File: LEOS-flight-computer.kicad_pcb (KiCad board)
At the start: 2 copper layers, 100 x 100 mm, 24 parts, among them J1 MicroFit_1x4, J2 MicroFit_1x4, J3 GPIO, J4 I2C Breakout, J5 SPI Breakout, U1 MCP2562FD, U2 MCP2518FD, Y1 40 MHz

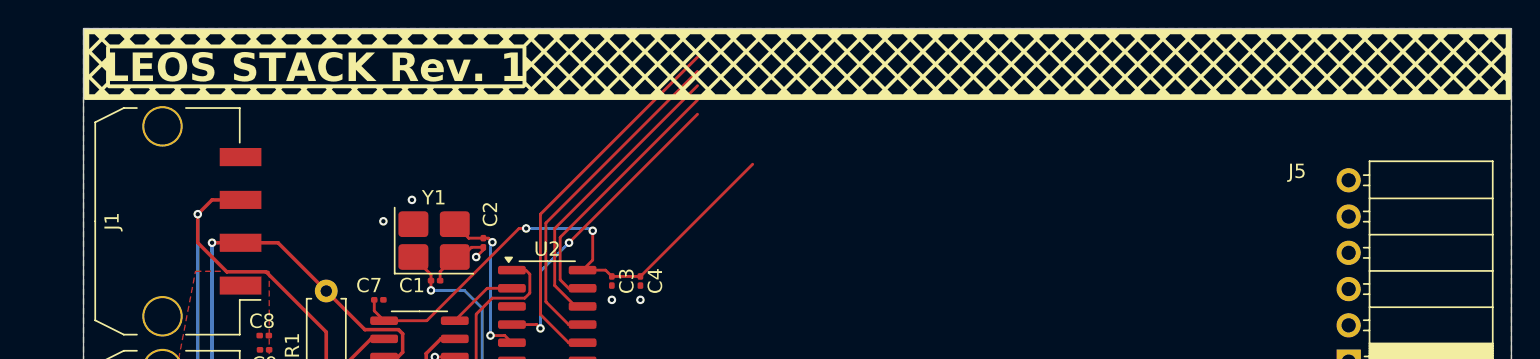
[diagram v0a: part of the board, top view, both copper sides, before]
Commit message: Change Silkscreen name to flight computer
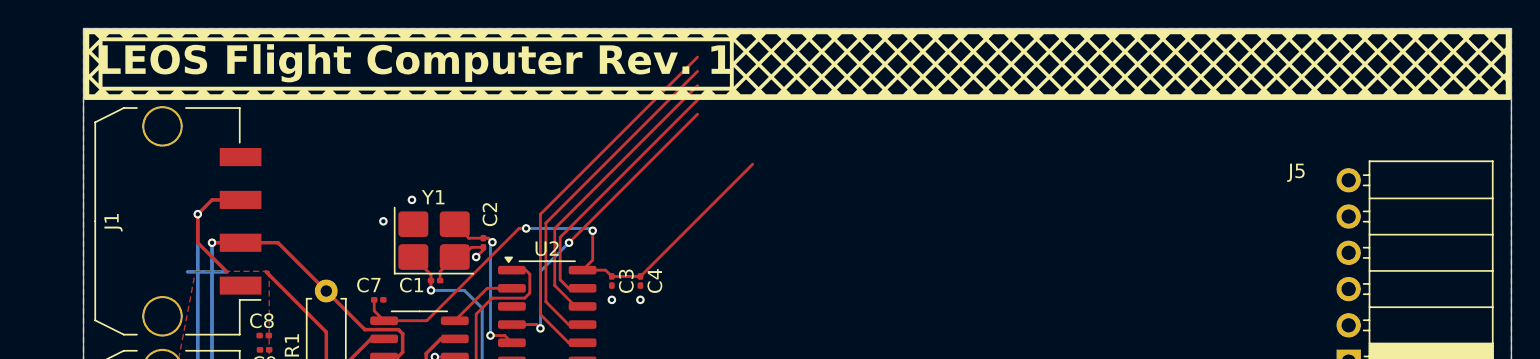
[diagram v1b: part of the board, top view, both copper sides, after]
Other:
- board text added: "LEOS Flight Computer Rev. 1"
- board text removed: "LEOS STACK Rev. 1"
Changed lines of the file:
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@@
 		(layer "Edge.Cuts")
 	)
-	(gr_text "LEOS STACK Rev. 1"
-		(at 116.25 52.75 0)
+	(gr_text "LEOS Flight Computer Rev. 1"
+		(at 123.25 52.25 0)
 		(layer "F.SilkS" knockout)
 		(effects
@@
 	)
 	(segment
-		(start 110.039 67.039)
-		(end 112.786 67.039)
-		(width 0.25)
-		(layer "F.Cu")
-		(net 12)
-	)
-	(segment
 		(start 108 65)
 		(end 110.039 67.039)
@@
 		(net 12)
 	)
+	(segment
+		(start 110.039 67.039)
+		(end 107.292 67.039)
+		(width 0.25)
+		(layer "B.Cu")
+		(net 12)
+	)

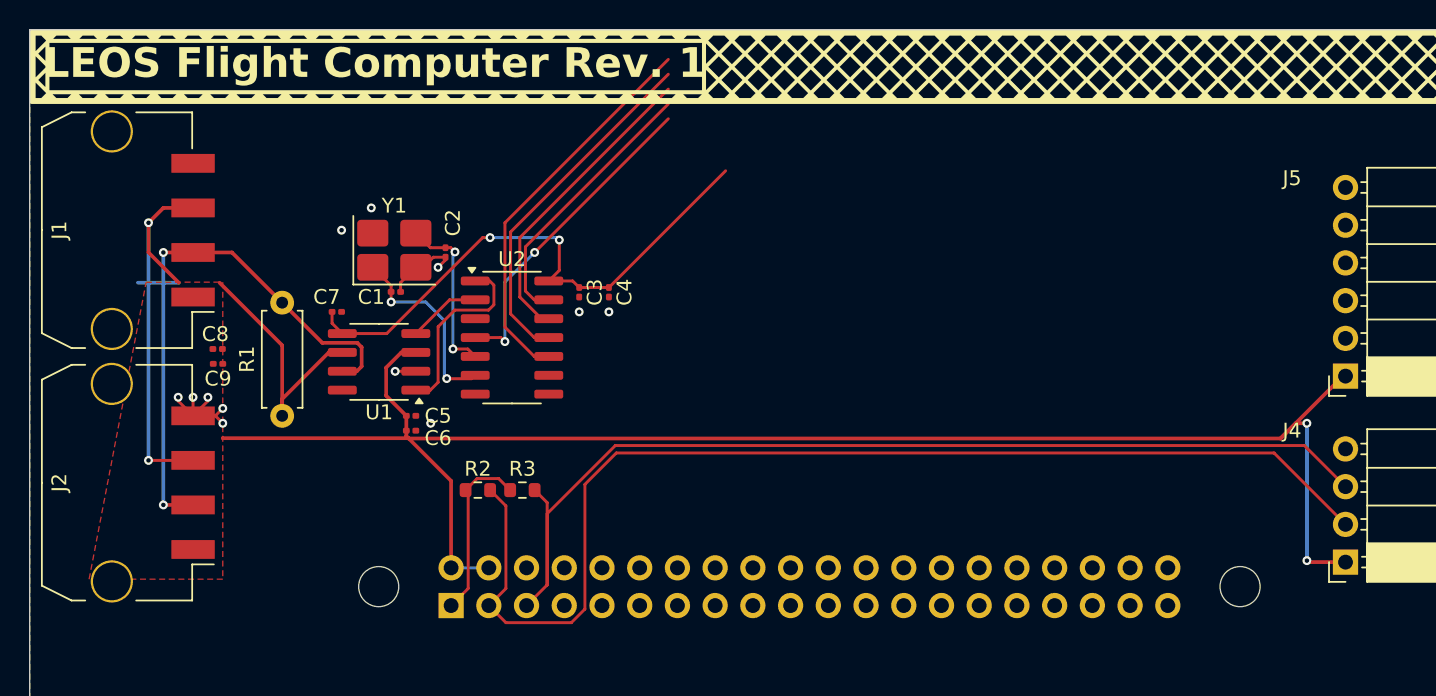
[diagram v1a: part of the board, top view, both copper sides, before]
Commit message: Corrected layout for flight computer with breakout headers routed
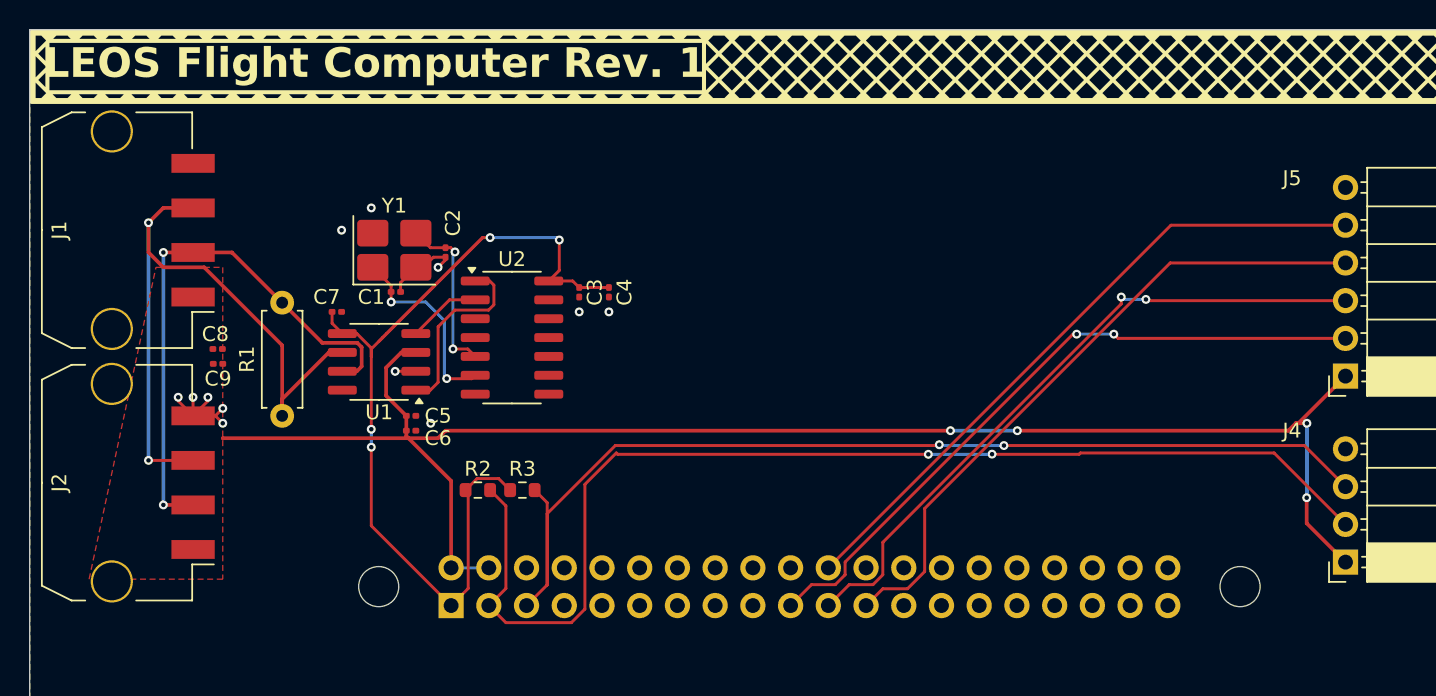
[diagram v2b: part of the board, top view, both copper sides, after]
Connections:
- J5 pad 3: GPIO09.SPI0/MISO -> GPIO9/SPI0.MISO
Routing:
- net GPIO10/SPI0.MOSI: track 0.00 -> 45.6 mm, vias 0 -> 2
- net GPIO9/SPI0.MISO: track 0.00 -> 45.1 mm, vias 0 -> 2
- net GPIO25: track 0.00 -> 44.4 mm
- net GPIO11/SPI0.SCLK: track 0.00 -> 44.3 mm
- net /CAN_SCK: track 26.3 -> 0.00 mm
- net /CAN_MOSI: track 23.8 -> 0.00 mm
- net /CAN_INT: track 21.7 -> 0.00 mm, vias 2 -> 0
- net /CAN_MISO: track 20.7 -> 0.00 mm
- net VDD: track 49.5 -> 69.2 mm, vias 2 -> 4
- net /CAN_CS: track 18.4 -> 0.00 mm
- net +5V: track 111.7 -> 108.8 mm, vias 2 -> 4
- net GPIO2/SDA1: track 78.5 -> 78.6 mm, vias 0 -> 2
- net GPIO3/SCL1: vias 0 -> 2

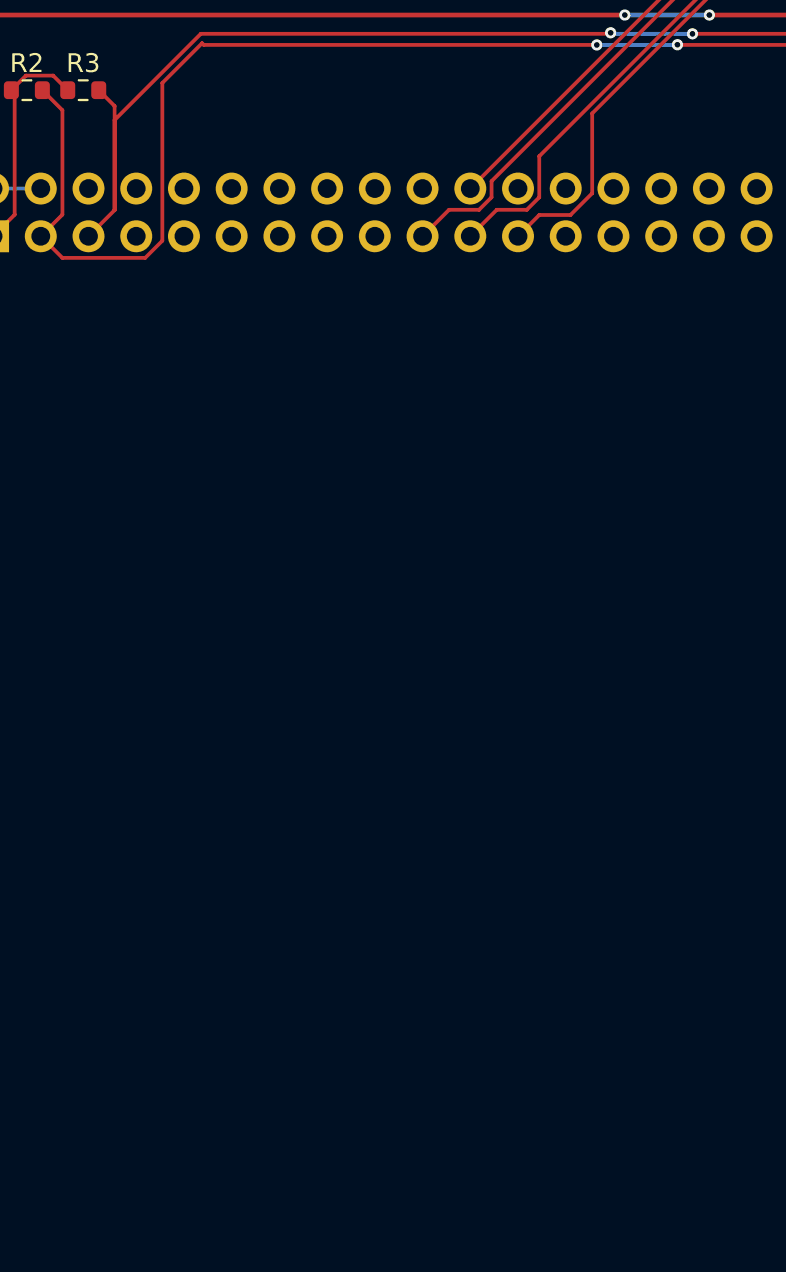
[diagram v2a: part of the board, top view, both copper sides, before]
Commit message: I routed and schematiced the gps model (SAM-M8Q).
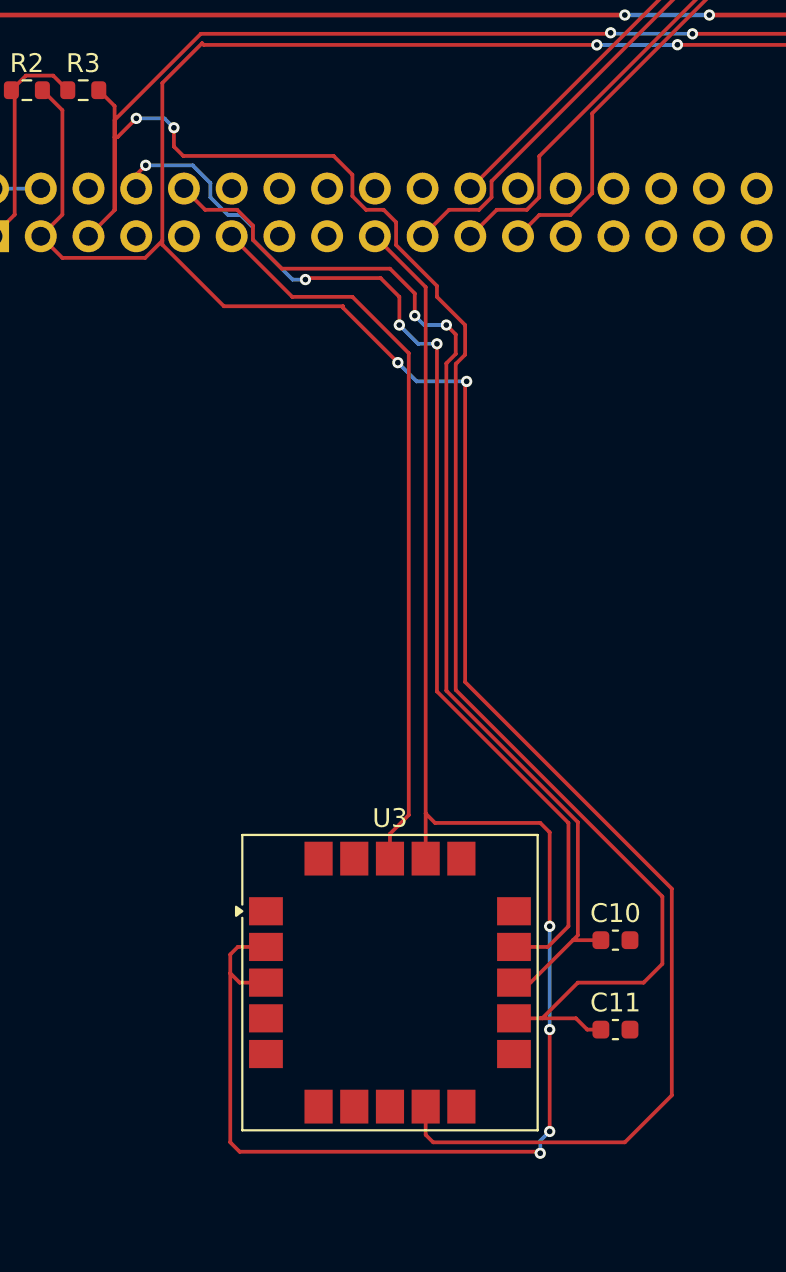
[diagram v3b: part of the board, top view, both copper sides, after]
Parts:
- added C10: 34pF, Capacitor_SMD:C_0603_1608Metric, F.Cu at (161.5, 126.2)
- added C11: 34pF, Capacitor_SMD:C_0603_1608Metric, F.Cu at (161.5, 131.0)
- added U3: SAM-M8Q, RF_GPS:ublox_SAM-M8Q, F.Cu at (149.5, 128.5)
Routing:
- net VDD: track 69.2 -> 158.6 mm, vias 4 -> 8
- net GPIO2/SDA1: track 78.6 -> 156.4 mm, vias 2 -> 4
- net GPIO3/SCL1: track 70.3 -> 147.5 mm, vias 2 -> 4
- net GPIO14/TXD0: track 0.00 -> 59.9 mm, vias 0 -> 4
- net GPIO15/RXD0: track 0.00 -> 59.8 mm, vias 0 -> 2
- net GPIO17: track 0.00 -> 39.3 mm

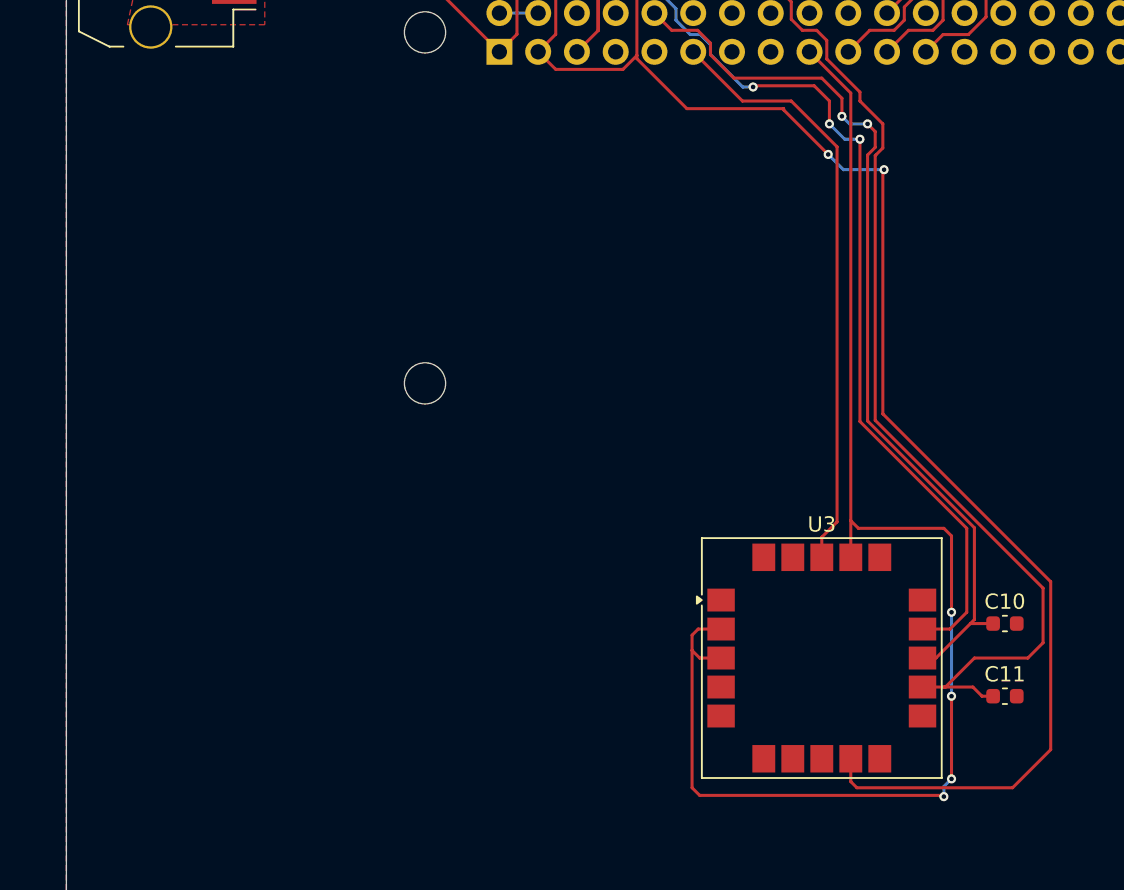
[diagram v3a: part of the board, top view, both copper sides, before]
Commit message: Routed and schematiced a coin cell bettery that is connected to V backup on the gps module
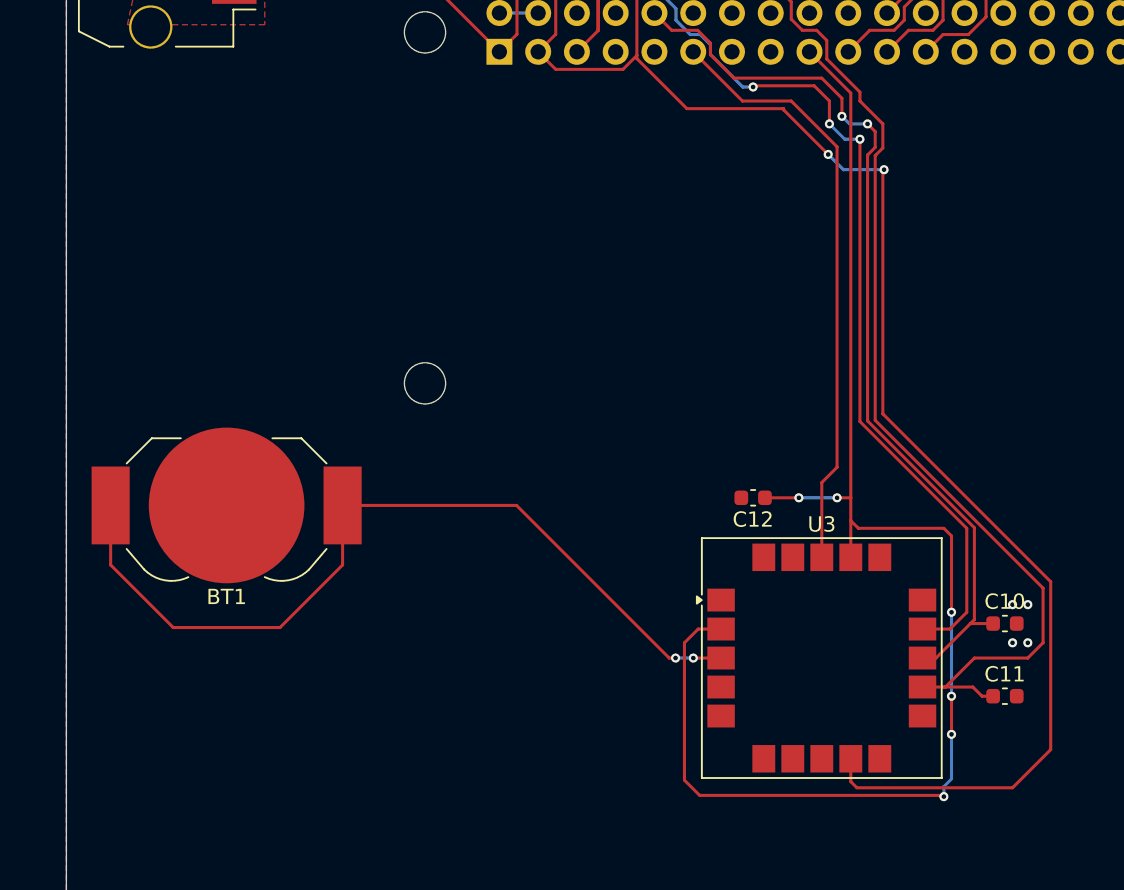
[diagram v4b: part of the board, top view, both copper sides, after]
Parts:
- added BT1: Battery_Cell, Battery:BatteryHolder_LINX_BAT-HLD-012-SMT, F.Cu at (110.5, 118.5)
- added C12: 0.1 uF, Capacitor_SMD:C_0603_1608Metric, F.Cu at (145.0, 118.0)
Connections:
- U3 pad 3: VDD -> Net-(BT1-+)
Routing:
- net Net-(BT1-+): track 0.00 -> 55.3 mm, vias 0 -> 2
- net VDD: track 158.6 -> 162.5 mm, vias 8 -> 10
- net GND: vias 12 -> 16

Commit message: Update
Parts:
- BT1: value Battery_Cell -> CR2032_Battery_Cell; footprint Battery:BatteryHolder_LINX_BAT-HLD-012-SMT -> CustomFootprints:BatteryHolder_SMD_MYOUNG_BS-08-B2AA010-R
- moved BT1 8.14 mm to (116.0, 124.5)
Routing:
- net Net-(BT1-+): track 55.3 -> 16.3 mm

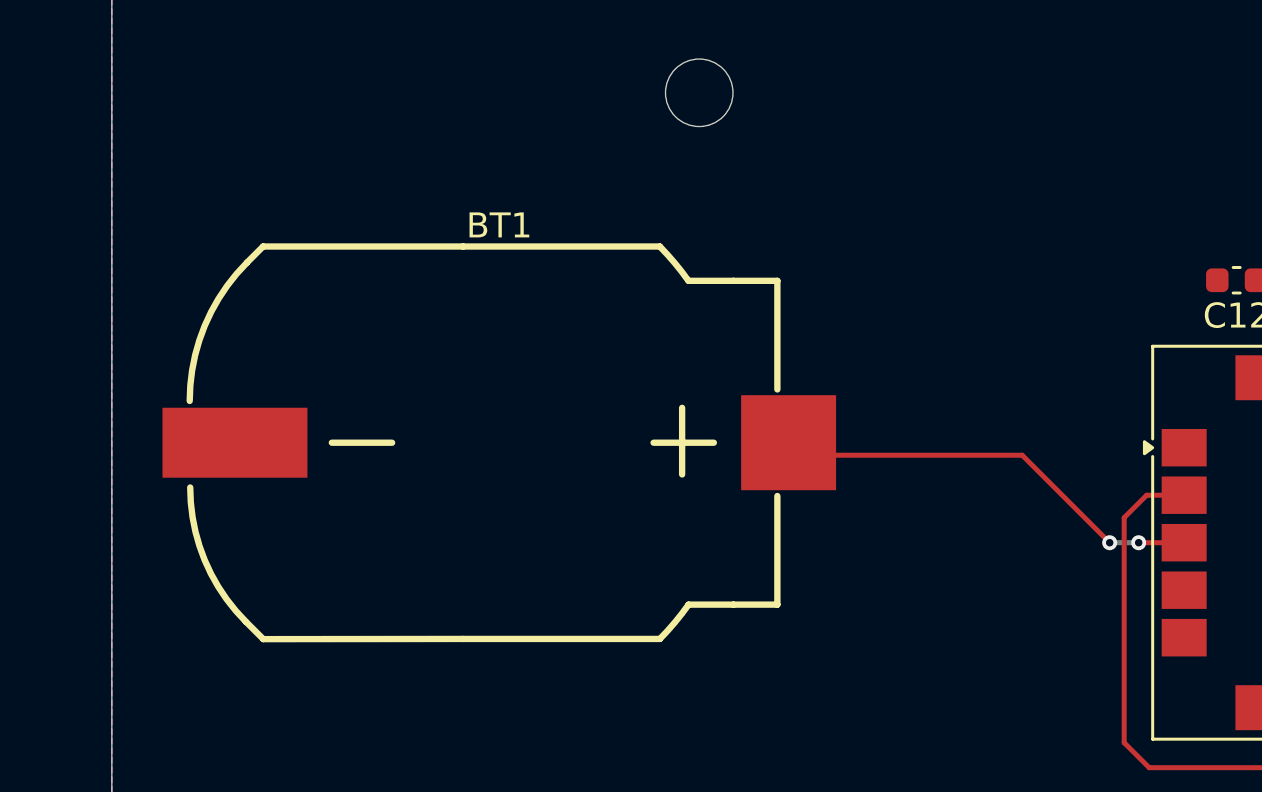
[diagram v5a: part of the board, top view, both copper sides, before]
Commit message: changed the battery holder to a better one
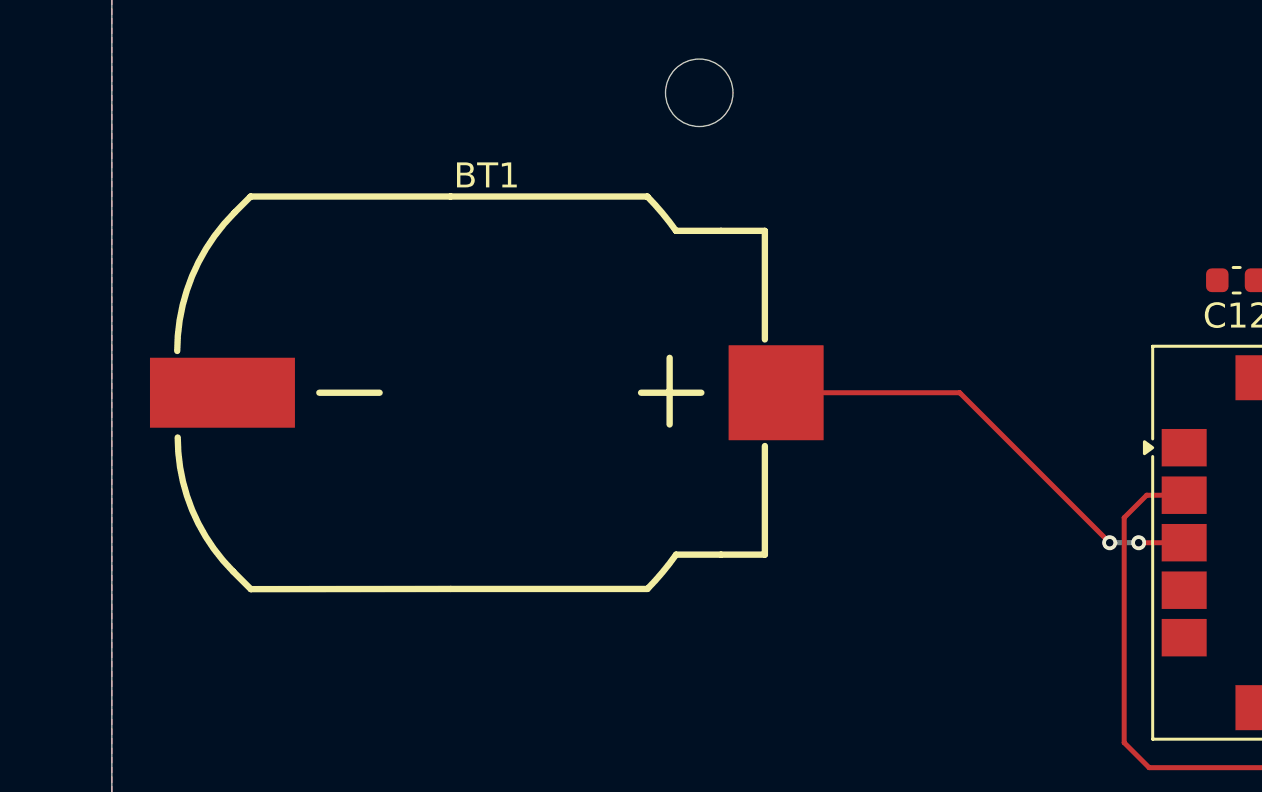
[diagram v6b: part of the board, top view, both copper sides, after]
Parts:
- moved BT1 2.06 mm to (115.5, 122.5)
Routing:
- net Net-(BT1-+): track 16.3 -> 18.8 mm
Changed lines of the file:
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@@
 	(footprint "CustomFootprints:BatteryHolder_SMD_MYOUNG_BS-08-B2AA010-R"
 		(layer "F.Cu")
-		(at 116 124.5)
+		(at 115.5 122.5)
 		(property "Reference" "BT1"
 			(at -0.5 -8.677 0)
@@
 	)
 	(segment
-		(start 128.075 125)
-		(end 136.42 125)
+		(start 133.92 122.5)
+		(end 139.92 128.5)
 		(width 0.2)
 		(layer "F.Cu")
@@
 	)
 	(segment
-		(start 136.42 125)
-		(end 139.92 128.5)
+		(start 126.575 122.5)
+		(end 133.92 122.5)
 		(width 0.2)
 		(layer "F.Cu")
